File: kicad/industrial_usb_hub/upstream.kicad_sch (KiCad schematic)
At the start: 1 part, among them J2 USB_C_Receptacle

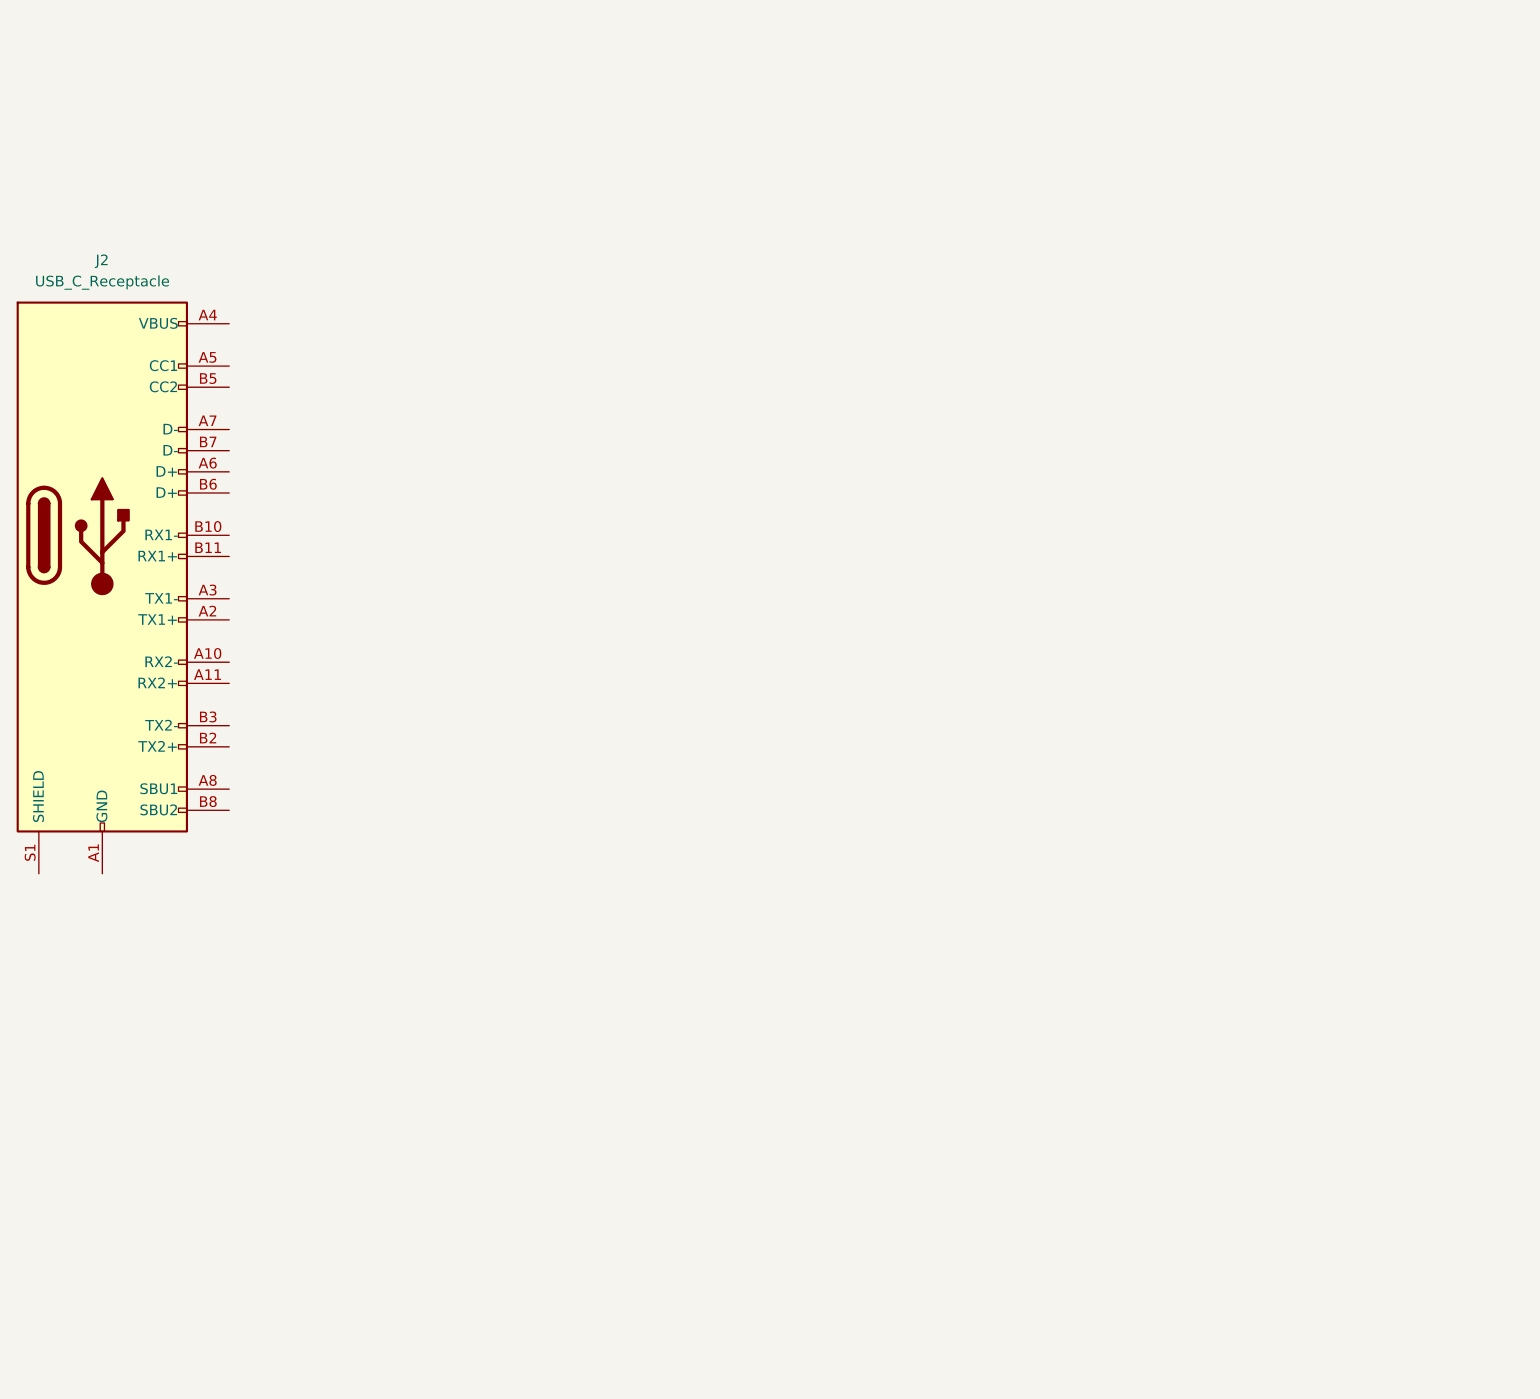
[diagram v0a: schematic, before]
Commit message: completed upstream circuit, moving on to power and downstream
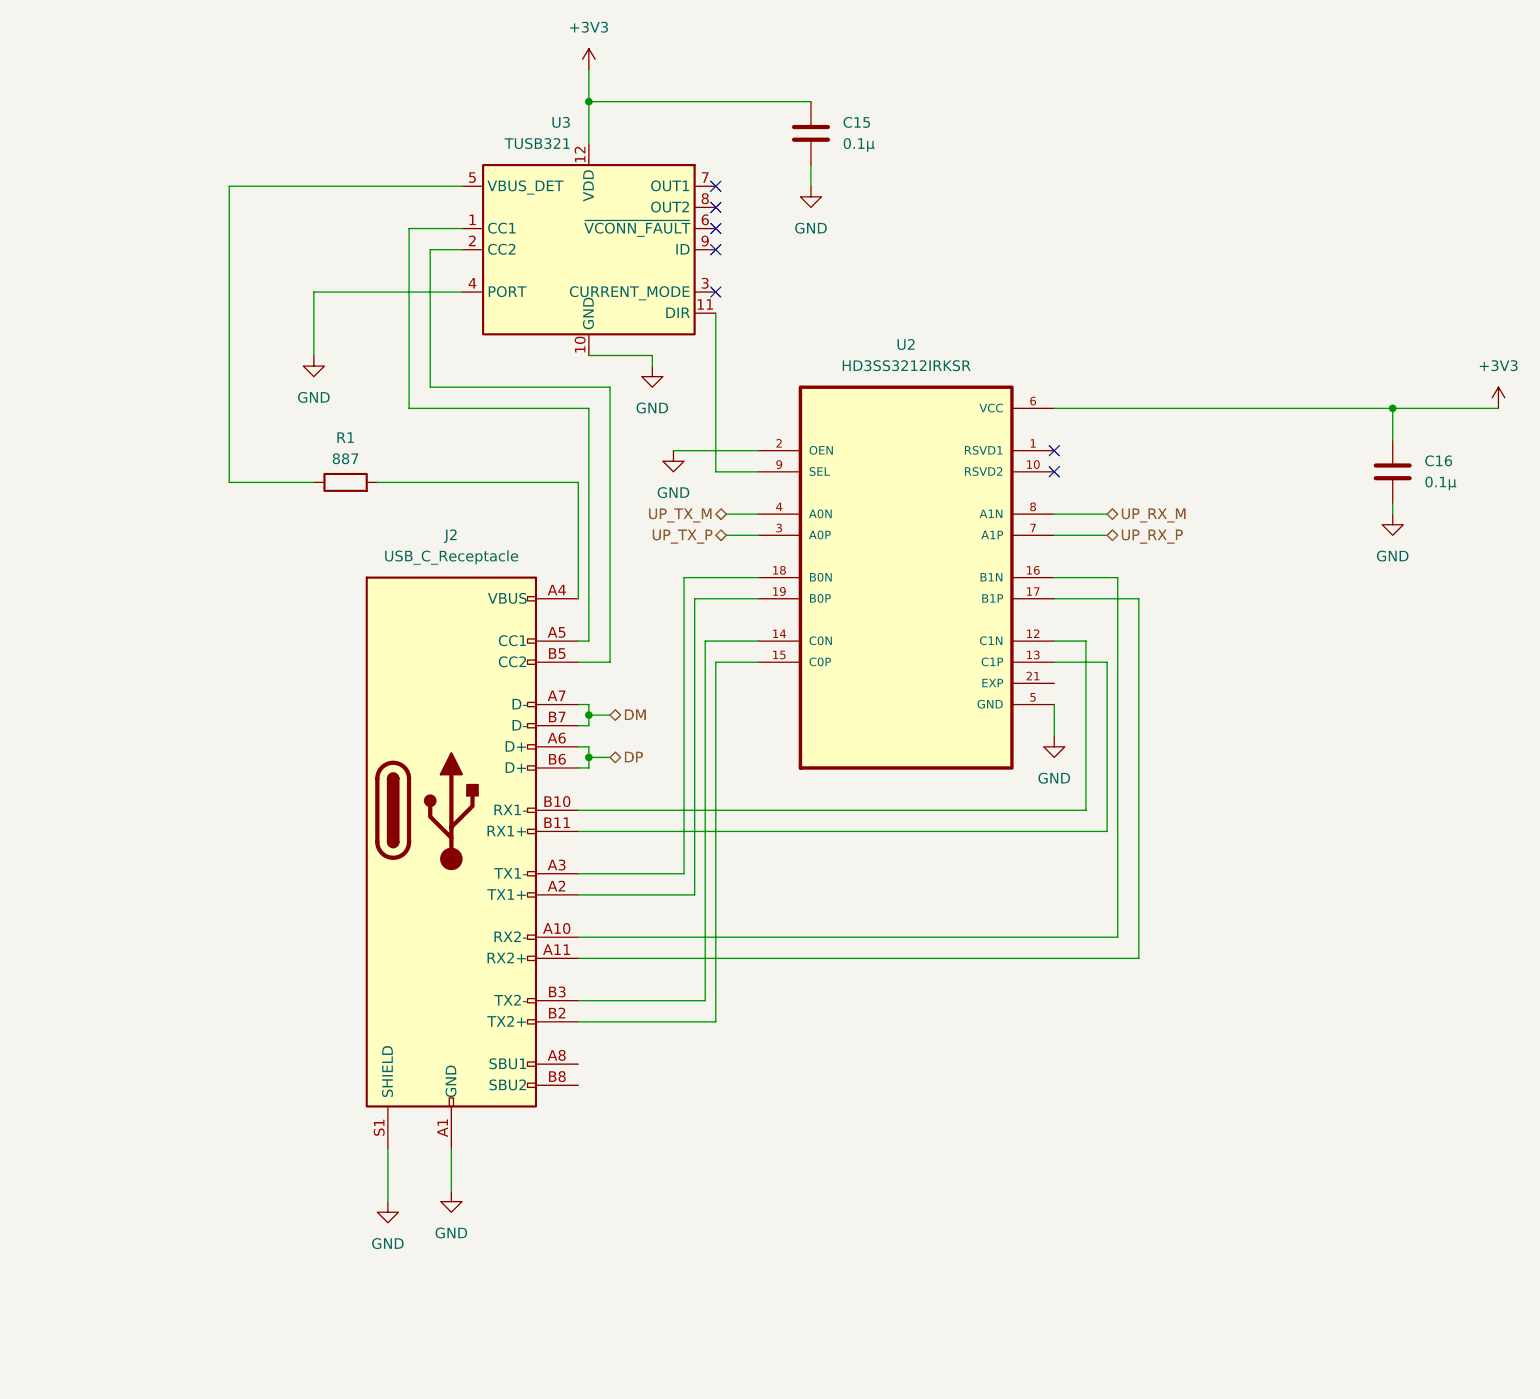
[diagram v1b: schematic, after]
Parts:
- added C15, C16: 0.1µ, Capacitor_SMD:C_0201_0603Metric, symbol Device:C
- added R1: 887, symbol Device:R
- added U2: HD3SS3212IRKSR, HD3SS3212IRKSR:QFN50P450X250X100-21N, symbol New_Library:HD3SS3212IRKSR
- added U3: TUSB321, Package_DFN_QFN:Texas_X2QFN-12_1.6x1.6mm_P0.4mm, symbol Interface_USB:TUSB321
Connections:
- net GND: now reaches J2.A1 (GND), J2.A12 (GND), J2.B1 (GND), J2.B12 (GND)
- net GND: now also J2.S1 (SHIELD), C15.2, C16.2, U2.11 (GND), U2.2 (OEN), U2.20 (GND), U2.5 (GND), U3.10 (GND), U3.4 (PORT)
- net at J2.A10 (RX2-): now also U2.16 (B1N)
- net at J2.A11 (RX2+): now also U2.17 (B1P)
- net at J2.A2 (TX1+): now also U2.19 (B0P)
- net at J2.A3 (TX1-): now also U2.18 (B0N)
- net at J2.A4 (VBUS), J2.A9 (VBUS), J2.B4 (VBUS)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: now also R1.2
- net at J2.A5 (CC1): now also U3.1 (CC1)
- net DP: now reaches J2.A6 (D+)
- net DP: now also J2.B6 (D+)
- net DM: now reaches J2.A7 (D-)
- net DM: now also J2.B7 (D-)
- net at J2.B10 (RX1-): now also U2.12 (C1N)
- net at J2.B11 (RX1+): now also U2.13 (C1P)
- net at J2.B2 (TX2+): now also U2.15 (C0P)
- net at J2.B3 (TX2-): now also U2.14 (C0N)
- net at J2.B5 (CC2): now also U3.2 (CC2)
- new net: U2.9 (SEL), U3.11 (DIR)
- new net: R1.1, U3.5 (VBUS_DET)
- new net +3V3: C15.1, C16.1, U2.6 (VCC), U3.12 (VDD)
- new net EXP: U2.21 (EXP), U2.21_1 (EXP), U2.21_2 (EXP), U2.21_3 (EXP)
- new net UP_RX_M: U2.8 (A1N)
- new net UP_RX_P: U2.7 (A1P)
- new net UP_TX_M: U2.4 (A0N)
- new net UP_TX_P: U2.3 (A0P)
- no-connect marks 0 -> 7
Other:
- moved on the sheet: J2

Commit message: completed schematic
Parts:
- added C22: 0.1µ, Capacitor_SMD:C_0201_0603Metric, symbol Device:C
- added R5: 887, symbol Device:R
- U2: footprint HD3SS3212IRKSR:QFN50P450X250X100-21N -> personal_library:QFN50P450X250X100-21N
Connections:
- net GND: now also C22.2, R5.2; no longer J2.S1 (SHIELD)
- net VBUS: now reaches J2.A4 (VBUS), J2.A9 (VBUS), J2.B4 (VBUS), J2.B9 (VBUS), R1.2
- net DM renamed UP_D_N
- net DP renamed UP_D_P
- net UP_RX_M renamed UP_RX_N
- net UP_TX_M renamed UP_TX_N
- new net: C22.1, J2.S1 (SHIELD), R5.1
- no-connect marks 7 -> 10
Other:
- title: (none) -> Upstream
- moved on the sheet: R1

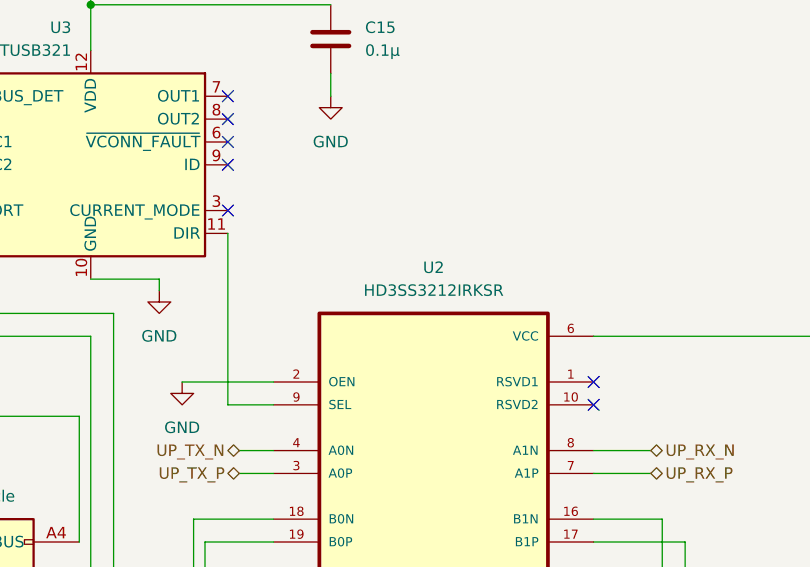
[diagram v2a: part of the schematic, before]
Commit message: assigned footprints
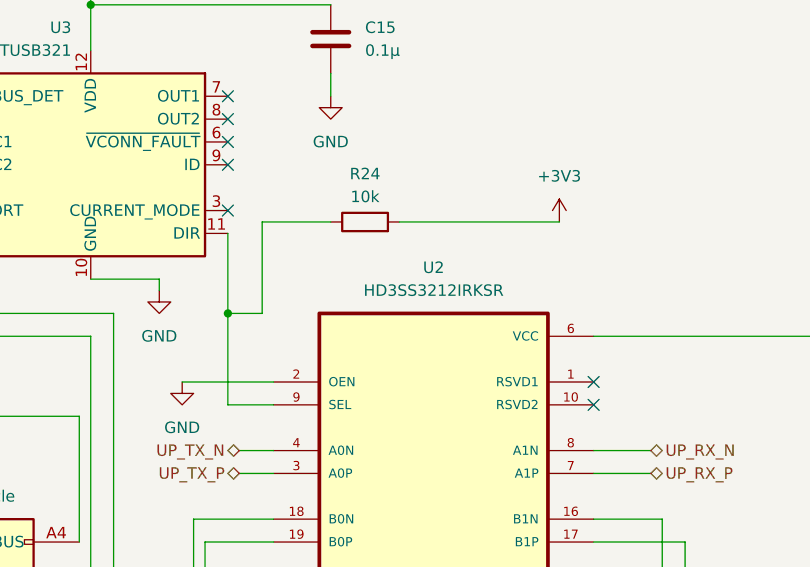
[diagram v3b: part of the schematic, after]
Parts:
- added R24: 10k, Resistor_SMD:R_0201_0603Metric, symbol Device:R
- J2: footprint (none) -> personal_library:BELFUSE_SS-52400-003
- R1, R5: footprint (none) -> Resistor_SMD:R_0201_0603Metric
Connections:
- net +3V3: now also R24.2
- net at U2.9 (SEL), U3.11 (DIR): now also R24.1
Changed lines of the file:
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@@
+	)
+	(junction
+		(at 140.97 58.42)
+		(diameter 0)
+		(color 0 0 0 0)
 	)
 	(junction
@@
 	(wire
 		(pts
+			(xy 140.97 58.42) (xy 140.97 68.58)
+		)
+		(stroke
+			(width 0)
+			(type default)
+		)
+	)
+	(wire
+		(pts
 			(xy 109.22 149.86) (xy 109.22 154.94)
 		)
@@
 	(wire
 		(pts
-			(xy 140.97 49.53) (xy 140.97 68.58)
+			(xy 140.97 49.53) (xy 140.97 58.42)
 		)
 		(stroke
@@
 	(wire
 		(pts
+			(xy 160.02 48.26) (xy 177.8 48.26)
+		)
+		(stroke
+			(width 0)
+			(type default)
+		)
+	)
+	(wire
+		(pts
 			(xy 83.82 69.85) (xy 82.55 69.85)
 		)
@@
 	(wire
 		(pts
+			(xy 144.78 48.26) (xy 144.78 58.42)
+		)
+		(stroke
+			(width 0)
+			(type default)
+		)
+	)
+	(wire
+		(pts
 			(xy 185.42 109.22) (xy 185.42 88.9)
 		)
@@
 	(wire
 		(pts
+			(xy 144.78 58.42) (xy 140.97 58.42)
+		)
+		(stroke
+			(width 0)
+			(type default)
+		)
+	)
+	(wire
+		(pts
 			(xy 189.23 81.28) (xy 181.61 81.28)
 		)
@@
 		(pts
 			(xy 222.25 60.96) (xy 234.95 60.96)
+		)
+		(stroke
+			(width 0)
+			(type default)
+		)
+	)
+	(wire
+		(pts
+			(xy 152.4 48.26) (xy 144.78 48.26)
 		)
 		(stroke
@@
 			)
 		)
-		(property "Footprint" ""
+		(property "Footprint" "Resistor_SMD:R_0201_0603Metric"
 			(at 87.63 71.628 90)
 			(effects
@@
 	)
 	(symbol
+		(lib_id "power:+3V3")
+		(at 177.8 48.26 0)
+		(unit 1)
+		(exclude_from_sim no)
+		(in_bom yes)
+		(on_board yes)
+		(dnp no)
+		(fields_autoplaced yes)
+		(property "Reference" "#PWR028"
+			(at 177.8 52.07 0)
+			(effects
+				(font
+					(size 1.27 1.27)
+				)
+				(hide yes)
+			)
+		)
+		(property "Value" "+3V3"
+			(at 177.8 43.18 0)
+			(effects
+				(font
+					(size 1.27 1.27)
+				)
+			)
+		)
+		(property "Footprint" ""
+			(at 177.8 48.26 0)
+			(effects
+				(font
+					(size 1.27 1.27)
+				)
+				(hide yes)
+			)
+		)
+		(property "Datasheet" ""
+			(at 177.8 48.26 0)
+			(effects
+				(font
+					(size 1.27 1.27)
+				)
+				(hide yes)
+			)
+		)
+		(property "Description" "Power symbol creates a global label with name \"+3V3\""
+			(at 177.8 48.26 0)
+			(effects
+				(font
+					(size 1.27 1.27)
+				)
+				(hide yes)
+			)
+		)
+		(pin "1"
+		)
+		(instances
+			(project "industrial_usb_hub"
+				(path "/2bdf928d-3bff-4ef5-bf26-63be25952cbb/ec29b23b-c3a8-42f0-ad46-1515655c12cf"
+					(reference "#PWR028")
+					(unit 1)
+				)
+			)
+		)
+	)
+	(symbol
 		(lib_id "Device:R")
 		(at 105.41 163.83 90)
@@
 			)
 		)
-		(property "Footprint" ""
+		(property "Footprint" "Resistor_SMD:R_0201_0603Metric"
 			(at 105.41 165.608 90)
 			(effects
@@
 	)
 	(symbol
+		(lib_id "Device:R")
+		(at 156.21 48.26 90)
+		(unit 1)
+		(exclude_from_sim no)
+		(in_bom yes)
+		(on_board yes)
+		(dnp no)
+		(property "Reference" "R24"
+			(at 156.21 42.926 90)
+			(effects
+				(font
+					(size 1.27 1.27)
+				)
+			)
+		)
+		(property "Value" "10k"
+			(at 156.21 45.466 90)
+			(effects
+				(font
+					(size 1.27 1.27)
+				)
+			)
+		)
+		(property "Footprint" "Resistor_SMD:R_0201_0603Metric"
+			(at 156.21 50.038 90)
+			(effects
+				(font
+					(size 1.27 1.27)
+				)
+				(hide yes)
+			)
+		)
+		(property "Datasheet" "~"
+			(at 156.21 48.26 0)
+			(effects
+				(font
+					(size 1.27 1.27)
+				)
+				(hide yes)
+			)
+		)
+		(property "Description" "Resistor"
+			(at 156.21 48.26 0)
+			(effects
+				(font
+					(size 1.27 1.27)
+				)
+				(hide yes)
+			)
+		)
+		(pin "1"
+		)
+		(pin "2"
+		)
+		(instances
+			(project "industrial_usb_hub"
+				(path "/2bdf928d-3bff-4ef5-bf26-63be25952cbb/ec29b23b-c3a8-42f0-ad46-1515655c12cf"
+					(reference "R24")
+					(unit 1)
+				)
+			)
+		)
+	)
+	(symbol
 		(lib_id "power:+3V3")
 		(at 125.73 20.32 0)
@@
 			)
 		)
-		(property "Footprint" ""
+		(property "Footprint" "personal_library:BELFUSE_SS-52400-003"
 			(at 113.03 109.22 0)
 			(effects

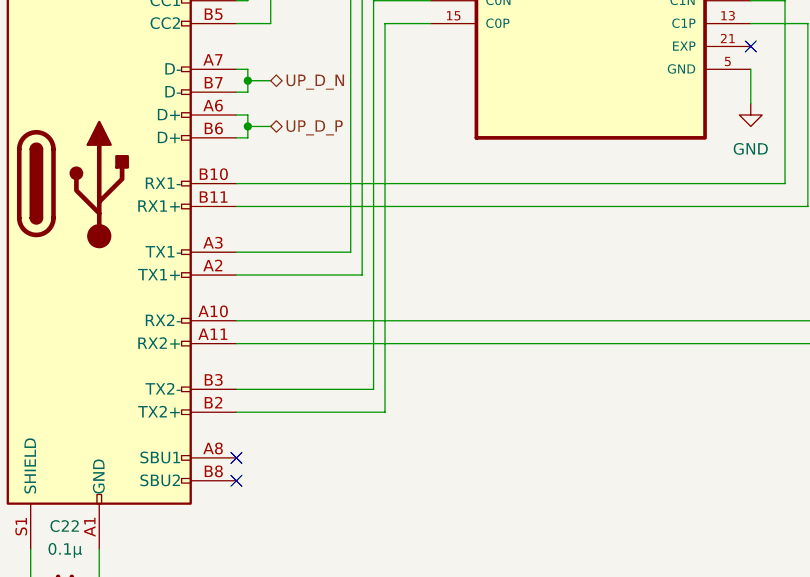
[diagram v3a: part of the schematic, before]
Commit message: moved on to pcb editor, chose component placements, groups, now needs routing, and bro routing superspeed just sucks
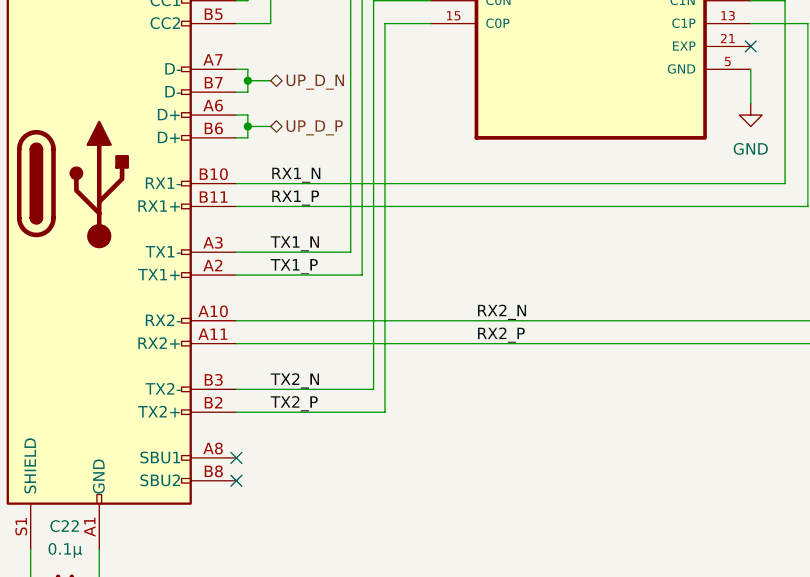
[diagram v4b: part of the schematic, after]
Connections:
- net EXP: no longer U2.21_1 (EXP), U2.21_2 (EXP), U2.21_3 (EXP)
- net RX1_N: now reaches J2.B10 (RX1-), U2.12 (C1N)
- net RX1_P: now reaches J2.B11 (RX1+), U2.13 (C1P)
- net TX2_N: now reaches J2.B3 (TX2-), U2.14 (C0N)
- net TX2_P: now reaches J2.B2 (TX2+), U2.15 (C0P)
- net RX2_N: now reaches J2.A10 (RX2-), U2.16 (B1N)
- net RX2_P: now reaches J2.A11 (RX2+), U2.17 (B1P)
- net TX1_N: now reaches J2.A3 (TX1-), U2.18 (B0N)
- net TX1_P: now reaches J2.A2 (TX1+), U2.19 (B0P)
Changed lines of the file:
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@@
+		)
+	)
+	(label "RX1_P"
+		(at 128.27 111.76 0)
+		(effects
+			(font
+				(size 1.27 1.27)
+			)
+			(justify left bottom)
+		)
+	)
+	(label "TX2_N"
+		(at 128.27 132.08 0)
+		(effects
+			(font
+				(size 1.27 1.27)
+			)
+			(justify left bottom)
+		)
+	)
+	(label "TX1_N"
+		(at 128.27 116.84 0)
+		(effects
+			(font
+				(size 1.27 1.27)
+			)
+			(justify left bottom)
+		)
+	)
+	(label "TX2_P"
+		(at 128.27 134.62 0)
+		(effects
+			(font
+				(size 1.27 1.27)
+			)
+			(justify left bottom)
+		)
+	)
+	(label "TX1_P"
+		(at 128.27 119.38 0)
+		(effects
+			(font
+				(size 1.27 1.27)
+			)
+			(justify left bottom)
+		)
+	)
+	(label "RX1_N"
+		(at 128.27 109.22 0)
+		(effects
+			(font
+				(size 1.27 1.27)
+			)
+			(justify left bottom)
+		)
+	)
+	(label "RX2_N"
+		(at 151.13 124.46 0)
+		(effects
+			(font
+				(size 1.27 1.27)
+			)
+			(justify left bottom)
+		)
+	)
+	(label "RX2_P"
+		(at 151.13 127 0)
+		(effects
+			(font
+				(size 1.27 1.27)
+			)
+			(justify left bottom)
 		)
 	)
@@
 		(pin "16"
 		)
-		(pin "21_3"
+		(pin "21"
 		)
 		(pin "11"
@@
 		(pin "12"
 		)
-		(pin "21_1"
+		(pin "21"
 		)
 		(pin "19"
@@
 		(pin "17"
 		)
-		(pin "21_2"
+		(pin "21"
 		)
 		(instances

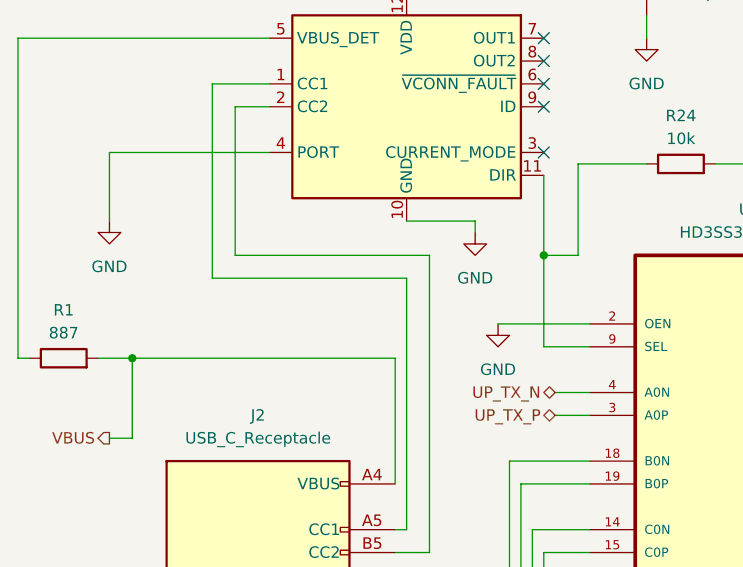
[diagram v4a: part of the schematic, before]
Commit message: added testpoints
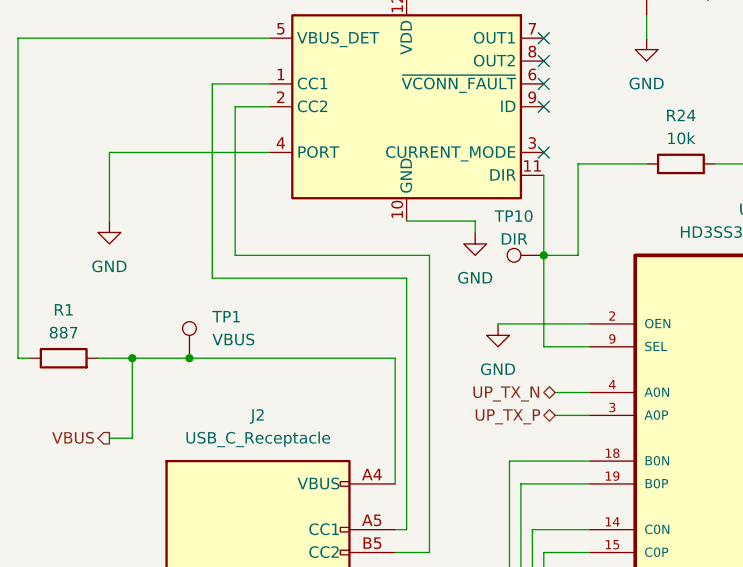
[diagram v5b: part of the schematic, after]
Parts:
- added TP1: VBUS, TestPoint:TestPoint_Pad_1.0x1.0mm, symbol Connector:TestPoint
- added TP10: DIR, TestPoint:TestPoint_Pad_1.0x1.0mm, symbol Connector:TestPoint
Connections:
- net VBUS: now also TP1.1
- net at R24.1, U2.9 (SEL), U3.11 (DIR): now also TP10.1
